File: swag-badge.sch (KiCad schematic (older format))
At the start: 10 parts, among them J1 OLED_1, J2 OLED_2, J3 Lolin32, J4 SAO_3, J5 SAO_1, J6 SAO_2, SW1 SW_Push, SW2 SW_Push

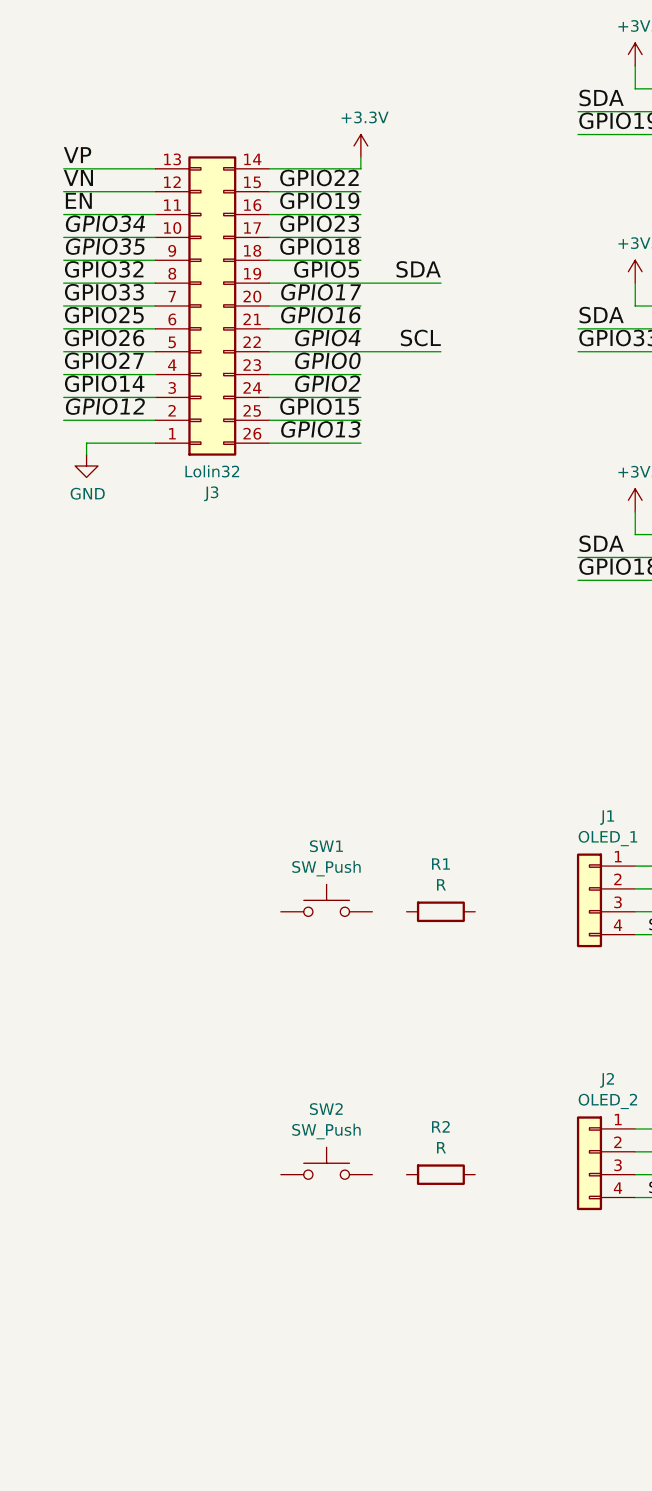
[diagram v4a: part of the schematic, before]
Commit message: Added buttons and sliders.
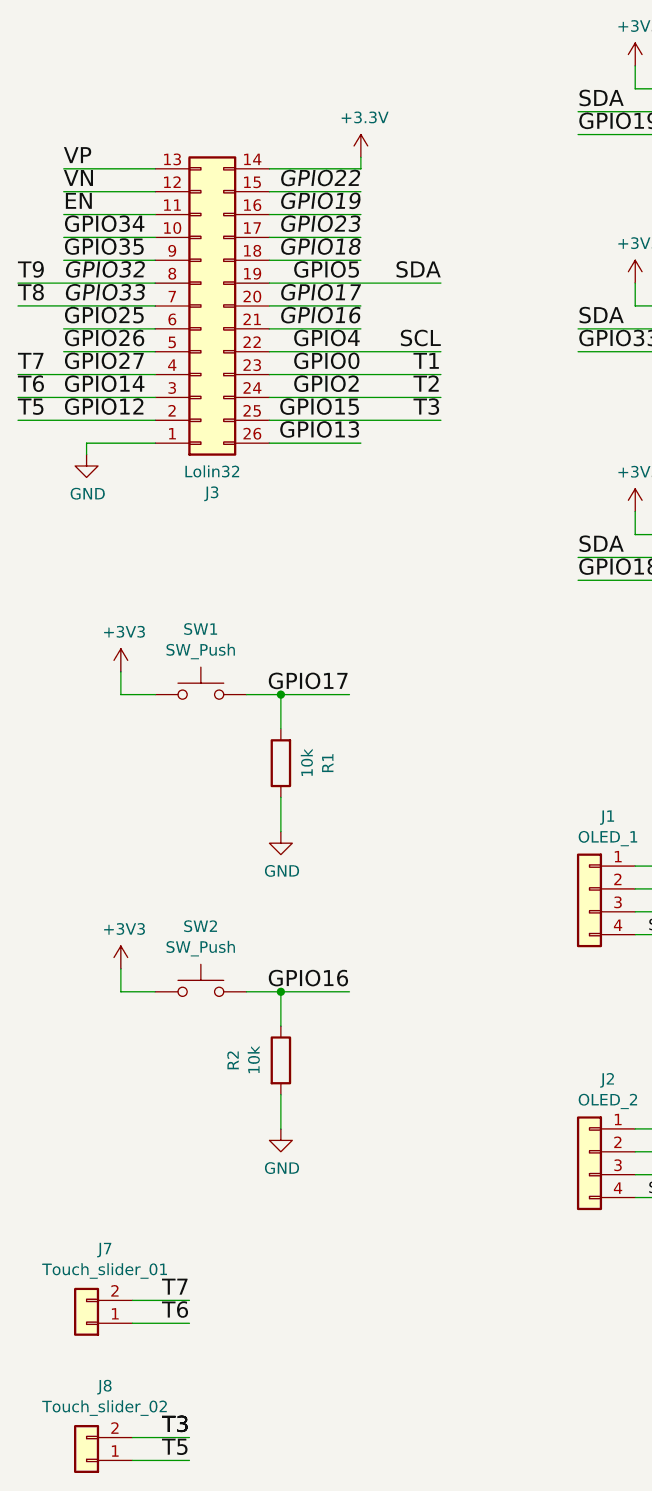
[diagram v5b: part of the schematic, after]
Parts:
- added J7: Touch_slider_01, libs:sense_short, symbol Connector_Generic:Conn_01x02
- added J8: Touch_slider_02, libs:sense_short, symbol Connector_Generic:Conn_01x02
- R1, R2: value R -> 10k
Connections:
- net +3V3: now also SW1.1, SW2.1
- net GND: now also R1.1, R2.2
- net GPIO12: now also J8.1 (Pin_1)
- net GPIO14: now also J7.1 (Pin_1)
- net GPIO15: now also J8.2 (Pin_2)
- net GPIO16: now also R2.1, SW2.2
- net GPIO17: now also R1.2, SW1.2
- net GPIO27: now also J7.2 (Pin_2)
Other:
- moved on the sheet: R1, R2, SW1, SW2
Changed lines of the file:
@@
 Wire Wire Line
 	2500 1400 2500 1350
-Wire Wire Line
-	1600 1900 1200 1900
-Text Label 1200 1900 0    70   ~ 0
+Text Label 1200 1900 0    70   Italic 0
 GPIO32
-Wire Wire Line
-	1600 2000 1200 2000
-Text Label 1200 2000 0    70   ~ 0
+Text Label 1200 2000 0    70   Italic 0
 GPIO33
 Wire Wire Line
@@
 Wire Wire Line
 	1600 1700 1200 1700
-Text Label 1200 1700 0    70   Italic 0
+Text Label 1200 1700 0    70   ~ 0
 GPIO34
 Wire Wire Line
 	1600 1800 1200 1800
-Text Label 1200 1800 0    70   Italic 0
+Text Label 1200 1800 0    70   ~ 0
 GPIO35
 Wire Wire Line
@@
 Text Label 1200 2200 0    70   ~ 0
 GPIO26
-Wire Wire Line
-	1600 2300 1200 2300
 Text Label 1200 2300 0    70   ~ 0
 GPIO27
-Wire Wire Line
-	1600 2400 1200 2400
 Text Label 1200 2400 0    70   ~ 0
 GPIO14
-Wire Wire Line
-	1600 2500 1200 2500
-Text Label 1200 2500 0    70   Italic 0
+Text Label 1200 2500 0    70   ~ 0
 GPIO12
 Wire Wire Line
 	2100 2600 2500 2600
-Text Label 2500 2600 2    70   Italic 0
+Text Label 2500 2600 2    70   ~ 0
 GPIO13
 $Comp
@@
 	1    0    0    -1
 $EndComp
-Text Label 2500 1500 2    70   ~ 0
+Text Label 2500 1500 2    70   Italic 0
 GPIO22
 Wire Wire Line
 	2100 1600 2500 1600
-Text Label 2500 1600 2    70   ~ 0
+Text Label 2500 1600 2    70   Italic 0
 GPIO19
 Wire Wire Line
 	2100 1700 2500 1700
-Text Label 2500 1700 2    70   ~ 0
-GPIO23
 Wire Wire Line
 	2100 1800 2500 1800
-Text Label 2500 1800 2    70   ~ 0
+Text Label 2500 1800 2    70   Italic 0
 GPIO18
 Text Label 2500 1900 2    70   ~ 0
@@
 Text Label 2500 2100 2    70   Italic 0
 GPIO16
-Text Label 2500 2200 2    70   Italic 0
+Text Label 2500 2200 2    70   ~ 0
 GPIO4
-Wire Wire Line
-	2100 2300 2500 2300
-Text Label 2500 2300 2    70   Italic 0
+Text Label 2500 2300 2    70   ~ 0
 GPIO0
-Wire Wire Line
-	2100 2400 2500 2400
-Text Label 2500 2400 2    70   Italic 0
+Text Label 2500 2400 2    70   ~ 0
 GPIO2
-Wire Wire Line
-	2100 2500 2500 2500
 Text Label 2500 2500 2    70   ~ 0
 GPIO15
@@
 L Switch:SW_Push SW1
 U 1 1 5F7A9FE9
-P 2350 4650
-F 0 "SW1" H 2350 4935 50  0000 C CNN
-F 1 "SW_Push" H 2350 4844 50  0000 C CNN
-F 2 "SwagBadge:SW_SPST_6x3mm" H 2350 4850 50  0001 C CNN
-F 3 "~" H 2350 4850 50  0001 C CNN
-	1    2350 4650
+P 1800 3700
+F 0 "SW1" H 1800 3985 50  0000 C CNN
+F 1 "SW_Push" H 1800 3894 50  0000 C CNN
+F 2 "SwagBadge:SW_SPST_6x3mm" H 1800 3900 50  0001 C CNN
+F 3 "~" H 1800 3900 50  0001 C CNN
+	1    1800 3700
 	1    0    0    -1
 $EndComp
@@
 L Device:R R1
 U 1 1 5F7B662C
-P 2850 4650
-F 0 "R1" V 2643 4650 50  0000 C CNN
-F 1 "R" V 2734 4650 50  0000 C CNN
-F 2 "Resistors_SMD:R_0805" V 2780 4650 50  0001 C CNN
-F 3 "~" H 2850 4650 50  0001 C CNN
-	1    2850 4650
-	0    1    1    0
+P 2150 4000
+F 0 "R1" V 1943 4000 50  0000 C CNN
+F 1 "10k" V 2034 4000 50  0000 C CNN
+F 2 "Resistors_SMD:R_0805" V 2080 4000 50  0001 C CNN
+F 3 "~" H 2150 4000 50  0001 C CNN
+	1    2150 4000
+	-1   0    0    1
 $EndComp
 $Comp
 L Switch:SW_Push SW2
 U 1 1 5F7BF1A3
-P 2350 5800
-F 0 "SW2" H 2350 6085 50  0000 C CNN
-F 1 "SW_Push" H 2350 5994 50  0000 C CNN
-F 2 "SwagBadge:SW_SPST_6x3mm" H 2350 6000 50  0001 C CNN
-F 3 "~" H 2350 6000 50  0001 C CNN
-	1    2350 5800
+P 1800 5000
+F 0 "SW2" H 1800 5285 50  0000 C CNN
+F 1 "SW_Push" H 1800 5194 50  0000 C CNN
+F 2 "SwagBadge:SW_SPST_6x3mm" H 1800 5200 50  0001 C CNN
+F 3 "~" H 1800 5200 50  0001 C CNN
+	1    1800 5000
 	1    0    0    -1
 $EndComp
@@
 L Device:R R2
 U 1 1 5F7BF1A9
-P 2850 5800
-F 0 "R2" V 2643 5800 50  0000 C CNN
-F 1 "R" V 2734 5800 50  0000 C CNN
-F 2 "Resistors_SMD:R_0805" V 2780 5800 50  0001 C CNN
-F 3 "~" H 2850 5800 50  0001 C CNN
-	1    2850 5800
-	0    1    1    0
-$EndComp
+P 2150 5300
+F 0 "R2" V 1943 5300 50  0000 C CNN
+F 1 "10k" V 2034 5300 50  0000 C CNN
+F 2 "Resistors_SMD:R_0805" V 2080 5300 50  0001 C CNN
+F 3 "~" H 2150 5300 50  0001 C CNN
+	1    2150 5300
+	1    0    0    -1
+$EndComp
+Text Label 2500 1700 2    70   Italic 0
+GPIO23
+Text Label 1000 2400 0    70   ~ 0
+T6
+Text Label 2850 2500 2    70   ~ 0
+T3
+Text Label 1000 2300 0    70   ~ 0
+T7
+Text Label 1000 1900 0    70   ~ 0
+T9
+Text Label 1000 2000 0    70   ~ 0
+T8
+Text Label 1000 2500 0    70   ~ 0
+T5
+Text Label 2850 2300 2    70   ~ 0
+T1
+Text Label 2850 2400 2    70   ~ 0
+T2
+Wire Wire Line
+	2100 2300 2850 2300
+Wire Wire Line
+	2100 2400 2850 2400
+Wire Wire Line
+	2100 2500 2850 2500
+Wire Wire Line
+	1000 2500 1600 2500
+Wire Wire Line
+	1000 2400 1600 2400
+Wire Wire Line
+	1000 2300 1600 2300
+Wire Wire Line
+	1000 2000 1600 2000
+Wire Wire Line
+	1000 1900 1600 1900
+$Comp
+L power:+3V3 #PWR0103
+U 1 1 5F7C311E
+P 1450 3600
+F 0 "#PWR0103" H 1450 3450 50  0001 C CNN
+F 1 "+3V3" H 1465 3773 50  0000 C CNN
+F 2 "" H 1450 3600 50  0001 C CNN
+F 3 "" H 1450 3600 50  0001 C CNN
+	1    1450 3600
+	1    0    0    -1
+$EndComp
+$Comp
+L power:GND #PWR0104
+U 1 1 5F7C3E3D
+P 2150 4300
+F 0 "#PWR0104" H 2150 4050 50  0001 C CNN
+F 1 "GND" H 2155 4127 50  0000 C CNN
+F 2 "" H 2150 4300 50  0001 C CNN
+F 3 "" H 2150 4300 50  0001 C CNN
+	1    2150 4300
+	1    0    0    -1
+$EndComp
+Wire Wire Line
+	1450 3600 1450 3700
+Wire Wire Line
+	1450 3700 1600 3700
+Wire Wire Line
+	2000 3700 2150 3700
+Wire Wire Line
+	2150 3700 2150 3850
+Wire Wire Line
+	2150 4150 2150 4300
+Wire Wire Line
+	2150 3700 2450 3700
+Connection ~ 2150 3700
+$Comp
+L power:+3V3 #PWR0113
+U 1 1 5F7CCF77
+P 1450 4900
+F 0 "#PWR0113" H 1450 4750 50  0001 C CNN
+F 1 "+3V3" H 1465 5073 50  0000 C CNN
+F 2 "" H 1450 4900 50  0001 C CNN
+F 3 "" H 1450 4900 50  0001 C CNN
+	1    1450 4900
+	1    0    0    -1
+$EndComp
+$Comp
+L power:GND #PWR0114
+U 1 1 5F7CDE40
+P 2150 5600
+F 0 "#PWR0114" H 2150 5350 50  0001 C CNN
+F 1 "GND" H 2155 5427 50  0000 C CNN
+F 2 "" H 2150 5600 50  0001 C CNN
+F 3 "" H 2150 5600 50  0001 C CNN
+	1    2150 5600
+	1    0    0    -1
+$EndComp
+Wire Wire Line
+	1450 4900 1450 5000
+Wire Wire Line
+	1450 5000 1600 5000
+Wire Wire Line
+	2000 5000 2150 5000
+Wire Wire Line
+	2150 5000 2150 5150
+Wire Wire Line
+	2150 5450 2150 5600
+Wire Wire Line
+	2150 5000 2450 5000
+Connection ~ 2150 5000
+Text Label 2450 3700 2    70   ~ 0
+GPIO17
+Text Label 2450 5000 2    70   ~ 0
+GPIO16
+Text Label 1750 6350 2    70   ~ 0
+T7
+Text Label 1750 6450 2    70   ~ 0
+T6
+Text Label 1750 7050 2    70   ~ 0
+T5
+Wire Wire Line
+	1500 6350 1750 6350
+Wire Wire Line
+	1500 6450 1750 6450
+Wire Wire Line
+	1500 7050 1750 7050
+$Comp
+L Connector_Generic:Conn_01x02 J7
+U 1 1 5F7E3B54
+P 1300 6450
+F 0 "J7" H 1218 6125 50  0000 C CNN
+F 1 "Touch_slider_01" H 1218 6216 50  0000 C CNN
+F 2 "libs:sense_short" H 1300 6450 50  0001 C CNN
+F 3 "~" H 1300 6450 50  0001 C CNN
+	1    1300 6450
+	-1   0    0    1
+$EndComp
+$Comp
+L Connector_Generic:Conn_01x02 J8
+U 1 1 5F7E4758
+P 1300 7050
+F 0 "J8" H 1218 6725 50  0000 C CNN
+F 1 "Touch_slider_02" H 1218 6816 50  0000 C CNN
+F 2 "libs:sense_short" H 1300 7050 50  0001 C CNN
+F 3 "~" H 1300 7050 50  0001 C CNN
+	1    1300 7050
+	-1   0    0    1
+$EndComp
+Text Label 1750 6950 2    70   ~ 0
+T3
+Text Label 1750 6950 2    70   ~ 0
+T3
+Wire Wire Line
+	1500 6950 1750 6950
 $EndSCHEMATC

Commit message: Sense sliders added to PCB
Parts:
- J7, J8: footprint libs:sense_short -> SwagBadge:sense_short
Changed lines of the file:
@@
 F 0 "J7" H 1218 6125 50  0000 C CNN
 F 1 "Touch_slider_01" H 1218 6216 50  0000 C CNN
-F 2 "libs:sense_short" H 1300 6450 50  0001 C CNN
+F 2 "SwagBadge:sense_short" H 1300 6450 50  0001 C CNN
 F 3 "~" H 1300 6450 50  0001 C CNN
 	1    1300 6450
@@
 F 0 "J8" H 1218 6725 50  0000 C CNN
 F 1 "Touch_slider_02" H 1218 6816 50  0000 C CNN
-F 2 "libs:sense_short" H 1300 7050 50  0001 C CNN
+F 2 "SwagBadge:sense_short" H 1300 7050 50  0001 C CNN
 F 3 "~" H 1300 7050 50  0001 C CNN
 	1    1300 7050

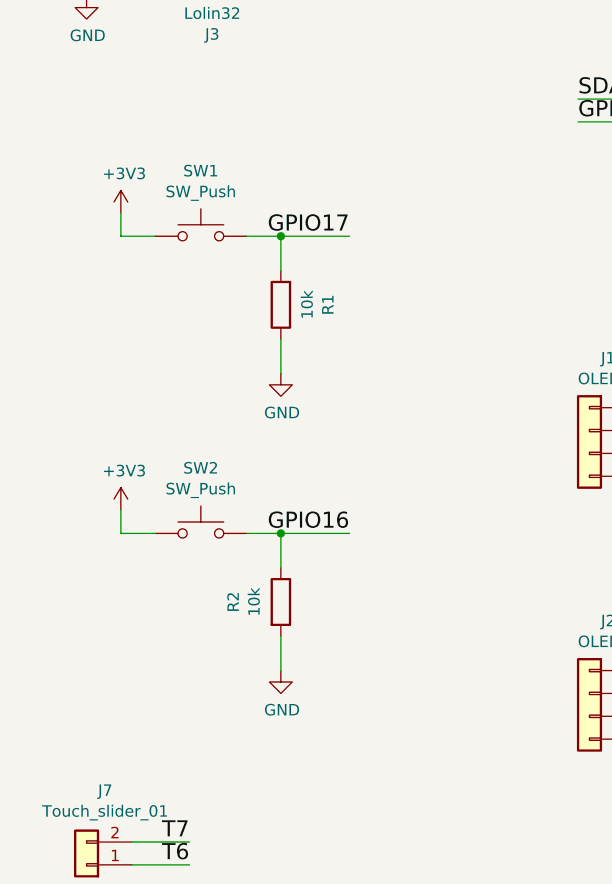
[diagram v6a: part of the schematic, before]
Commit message: switched to internal pullups for buttons
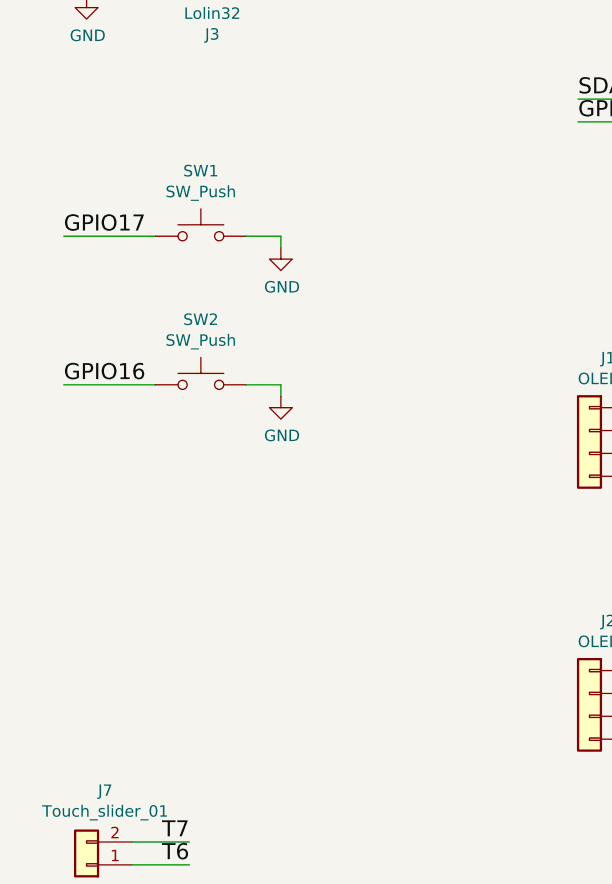
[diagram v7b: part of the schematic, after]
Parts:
- removed R1, R2: 10k, Resistors_SMD:R_0805, symbol Device:R
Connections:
- net +3V3: no longer SW1.1, SW2.1
- net GND: now also SW1.2, SW2.2
- net GPIO16: now also SW2.1; no longer SW2.2
- net GPIO17: now also SW1.1; no longer SW1.2
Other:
- moved on the sheet: SW2
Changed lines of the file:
@@
-$EndComp
-$Comp
-L Device:R R1
-U 1 1 5F7B662C
-P 2150 4000
-F 0 "R1" V 1943 4000 50  0000 C CNN
-F 1 "10k" V 2034 4000 50  0000 C CNN
-F 2 "Resistors_SMD:R_0805" V 2080 4000 50  0001 C CNN
-F 3 "~" H 2150 4000 50  0001 C CNN
-	1    2150 4000
-	-1   0    0    1
 $EndComp
 $Comp
 L Switch:SW_Push SW2
 U 1 1 5F7BF1A3
-P 1800 5000
-F 0 "SW2" H 1800 5285 50  0000 C CNN
-F 1 "SW_Push" H 1800 5194 50  0000 C CNN
-F 2 "SwagBadge:SW_SPST_6x3mm" H 1800 5200 50  0001 C CNN
-F 3 "~" H 1800 5200 50  0001 C CNN
-	1    1800 5000
-	1    0    0    -1
-$EndComp
-$Comp
-L Device:R R2
-U 1 1 5F7BF1A9
-P 2150 5300
-F 0 "R2" V 1943 5300 50  0000 C CNN
-F 1 "10k" V 2034 5300 50  0000 C CNN
-F 2 "Resistors_SMD:R_0805" V 2080 5300 50  0001 C CNN
-F 3 "~" H 2150 5300 50  0001 C CNN
-	1    2150 5300
+P 1800 4350
+F 0 "SW2" H 1800 4635 50  0000 C CNN
+F 1 "SW_Push" H 1800 4544 50  0000 C CNN
+F 2 "SwagBadge:SW_SPST_6x3mm" H 1800 4550 50  0001 C CNN
+F 3 "~" H 1800 4550 50  0001 C CNN
+	1    1800 4350
 	1    0    0    -1
 $EndComp
@@
 	1000 1900 1600 1900
 $Comp
-L power:+3V3 #PWR0103
-U 1 1 5F7C311E
-P 1450 3600
-F 0 "#PWR0103" H 1450 3450 50  0001 C CNN
-F 1 "+3V3" H 1465 3773 50  0000 C CNN
-F 2 "" H 1450 3600 50  0001 C CNN
-F 3 "" H 1450 3600 50  0001 C CNN
-	1    1450 3600
-	1    0    0    -1
-$EndComp
-$Comp
 L power:GND #PWR0104
 U 1 1 5F7C3E3D
-P 2150 4300
-F 0 "#PWR0104" H 2150 4050 50  0001 C CNN
-F 1 "GND" H 2155 4127 50  0000 C CNN
-F 2 "" H 2150 4300 50  0001 C CNN
-F 3 "" H 2150 4300 50  0001 C CNN
-	1    2150 4300
+P 2150 3750
+F 0 "#PWR0104" H 2150 3500 50  0001 C CNN
+F 1 "GND" H 2155 3577 50  0000 C CNN
+F 2 "" H 2150 3750 50  0001 C CNN
+F 3 "" H 2150 3750 50  0001 C CNN
+	1    2150 3750
 	1    0    0    -1
 $EndComp
 Wire Wire Line
-	1450 3600 1450 3700
-Wire Wire Line
-	1450 3700 1600 3700
-Wire Wire Line
 	2000 3700 2150 3700
 Wire Wire Line
-	2150 3700 2150 3850
+	2150 3700 2150 3750
 Wire Wire Line
-	2150 4150 2150 4300
-Wire Wire Line
-	2150 3700 2450 3700
-Connection ~ 2150 3700
-$Comp
-L power:+3V3 #PWR0113
-U 1 1 5F7CCF77
-P 1450 4900
-F 0 "#PWR0113" H 1450 4750 50  0001 C CNN
-F 1 "+3V3" H 1465 5073 50  0000 C CNN
-F 2 "" H 1450 4900 50  0001 C CNN
-F 3 "" H 1450 4900 50  0001 C CNN
-	1    1450 4900
-	1    0    0    -1
-$EndComp
+	1200 3700 1600 3700
 $Comp
 L power:GND #PWR0114
 U 1 1 5F7CDE40
-P 2150 5600
-F 0 "#PWR0114" H 2150 5350 50  0001 C CNN
-F 1 "GND" H 2155 5427 50  0000 C CNN
-F 2 "" H 2150 5600 50  0001 C CNN
-F 3 "" H 2150 5600 50  0001 C CNN
-	1    2150 5600
+P 2150 4400
+F 0 "#PWR0114" H 2150 4150 50  0001 C CNN
+F 1 "GND" H 2155 4227 50  0000 C CNN
+F 2 "" H 2150 4400 50  0001 C CNN
+F 3 "" H 2150 4400 50  0001 C CNN
+	1    2150 4400
 	1    0    0    -1
 $EndComp
 Wire Wire Line
-	1450 4900 1450 5000
+	2000 4350 2150 4350
 Wire Wire Line
-	1450 5000 1600 5000
+	2150 4350 2150 4400
 Wire Wire Line
-	2000 5000 2150 5000
-Wire Wire Line
-	2150 5000 2150 5150
-Wire Wire Line
-	2150 5450 2150 5600
-Wire Wire Line
-	2150 5000 2450 5000
-Connection ~ 2150 5000
-Text Label 2450 3700 2    70   ~ 0
+	1200 4350 1600 4350
+Text Label 1200 3700 0    70   ~ 0
 GPIO17
-Text Label 2450 5000 2    70   ~ 0
+Text Label 1200 4350 0    70   ~ 0
 GPIO16
 Text Label 1750 6350 2    70   ~ 0

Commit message: New Touch Slider
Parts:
- J7, J8: footprint SwagBadge:sense_short -> SwagBadge:Touch_Slider
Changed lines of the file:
@@
 F 0 "J7" H 1218 6125 50  0000 C CNN
 F 1 "Touch_slider_01" H 1218 6216 50  0000 C CNN
-F 2 "SwagBadge:sense_short" H 1300 6450 50  0001 C CNN
+F 2 "SwagBadge:Touch_Slider" H 1300 6450 50  0001 C CNN
 F 3 "~" H 1300 6450 50  0001 C CNN
 	1    1300 6450
@@
 F 0 "J8" H 1218 6725 50  0000 C CNN
 F 1 "Touch_slider_02" H 1218 6816 50  0000 C CNN
-F 2 "SwagBadge:sense_short" H 1300 7050 50  0001 C CNN
+F 2 "SwagBadge:Touch_Slider" H 1300 7050 50  0001 C CNN
 F 3 "~" H 1300 7050 50  0001 C CNN
 	1    1300 7050
